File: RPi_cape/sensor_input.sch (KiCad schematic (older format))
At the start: 39 parts, among them U5 LM2903, U6 LMC7101B, U7 LMC7101B

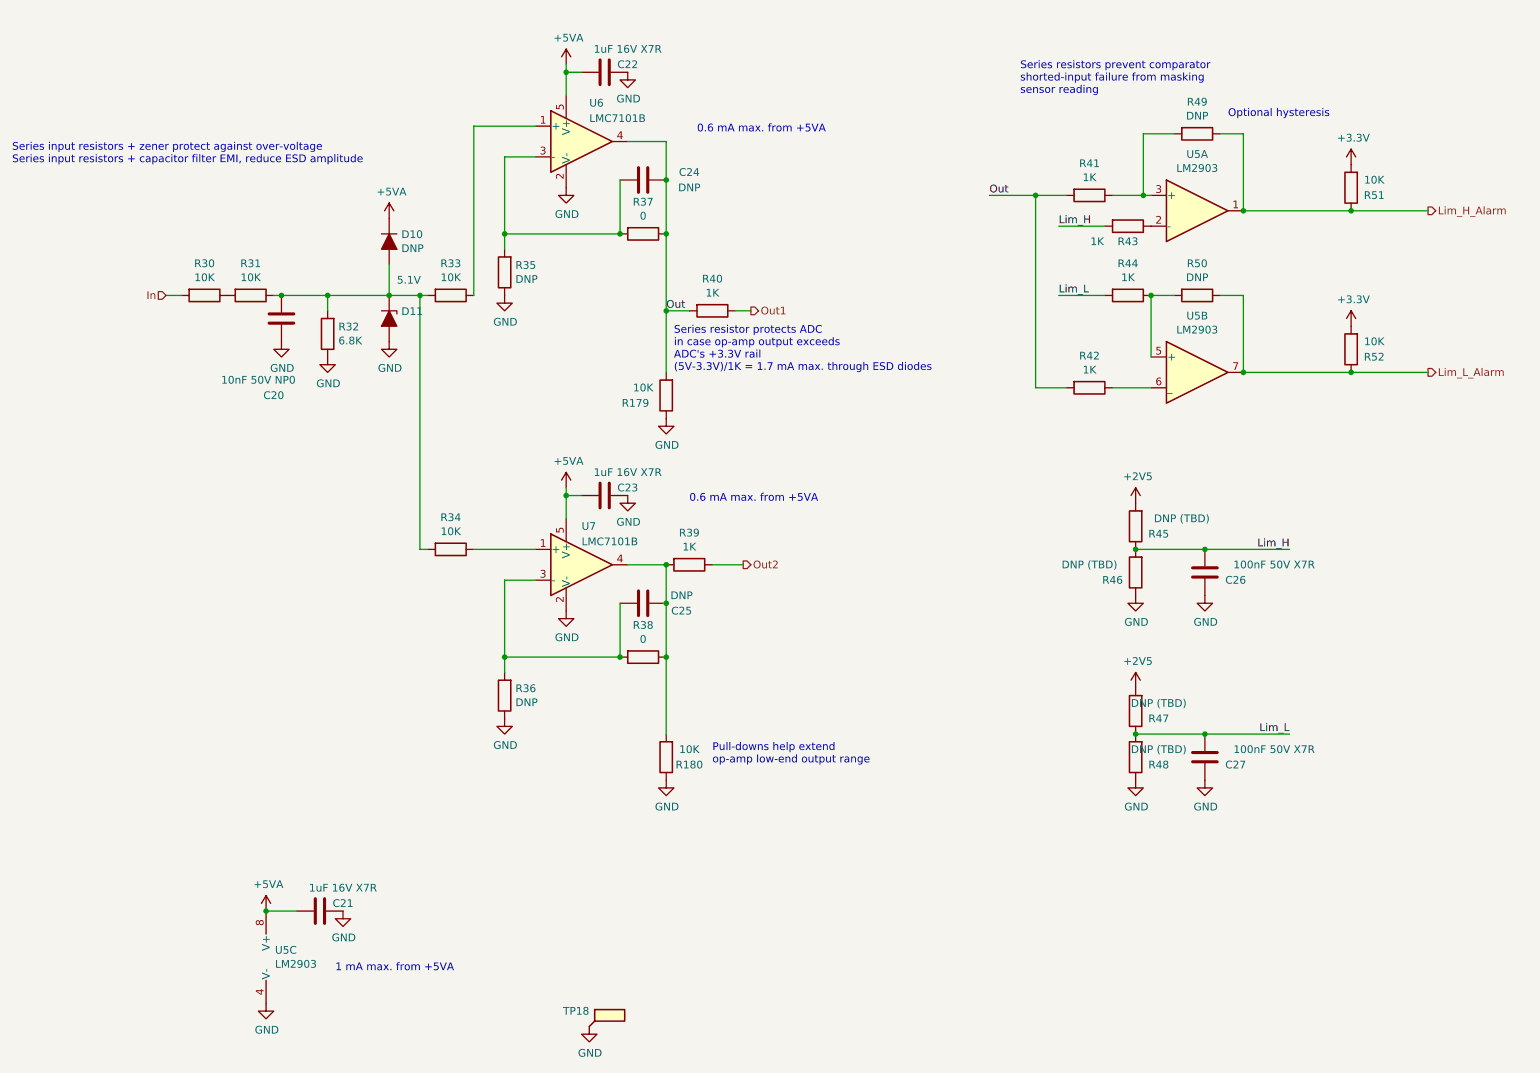
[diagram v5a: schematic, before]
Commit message: Safety additions
Switched CPLD_ADC7 to +24V monitoring (from +5V monitoring), and added CPLD ~Bat_On digital input(s) to know when it's running from backup battery, to cover low-input-voltage edge cases
Added series 1K resistors (R226-231) on CPLD<->RPi Comms1-6 lines, to protect CPLD in case of overvoltage from RPi failure
Added optional input TVS D23 to handle sustained over-voltage or large surges
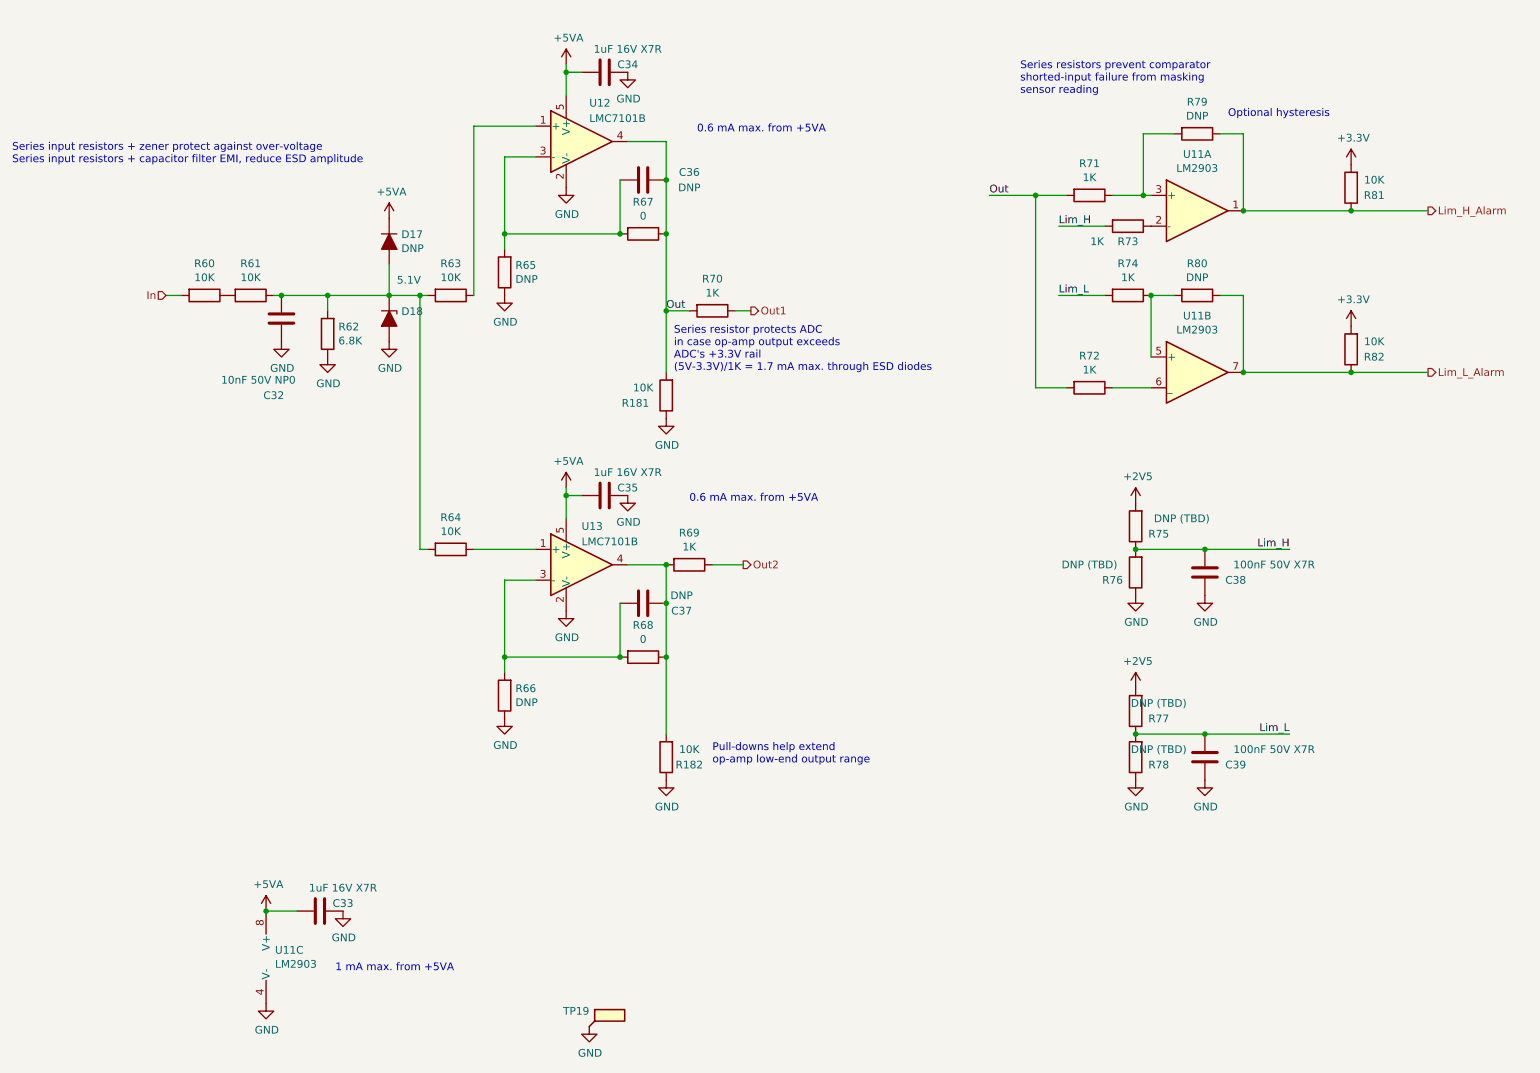
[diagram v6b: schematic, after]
